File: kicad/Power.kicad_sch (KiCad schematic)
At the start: 40 parts, among them J201 USB_C_2.0, J202 Conn_01x03, U201 RP509Z331B, U202 RP509Z251B, U203 TPS25750DRJK

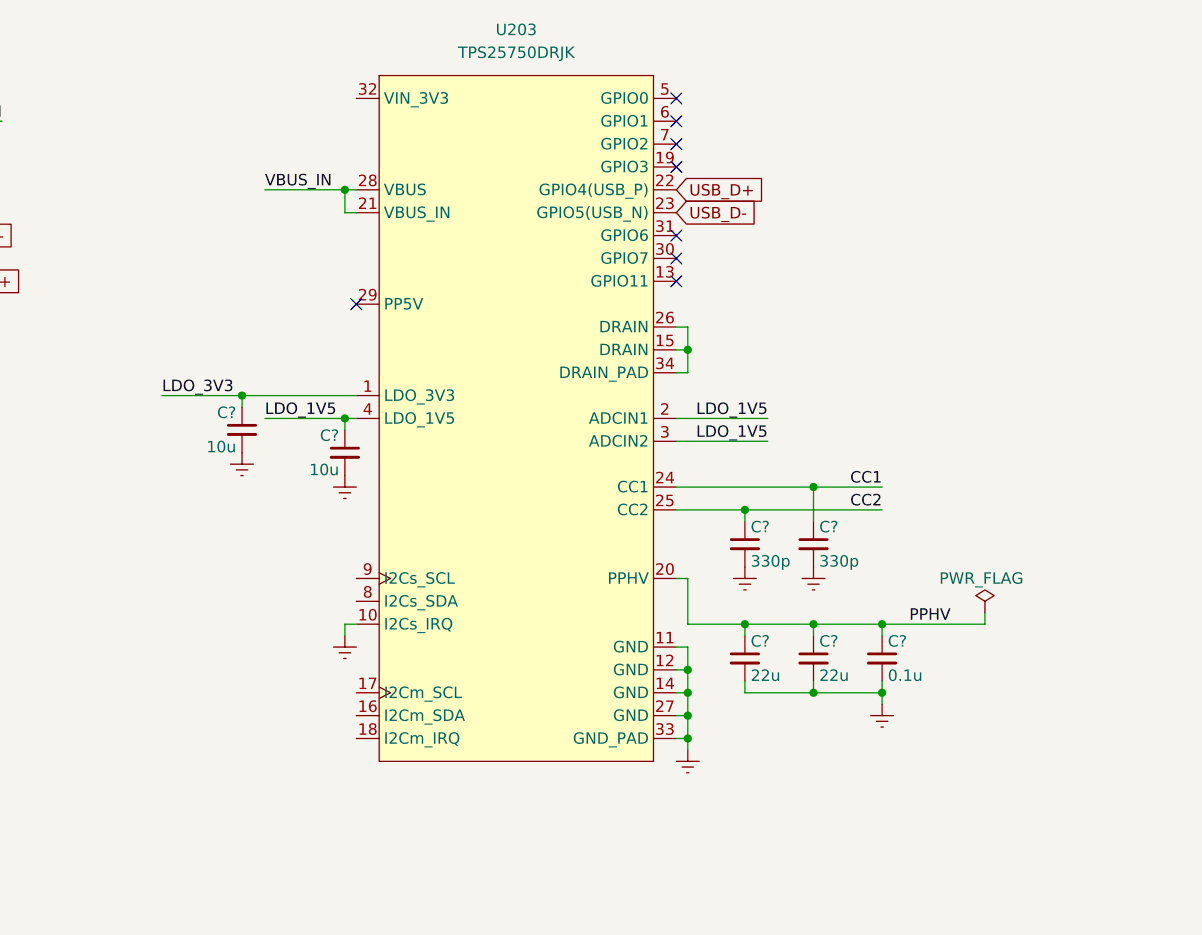
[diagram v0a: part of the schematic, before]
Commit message: rename kicad project files
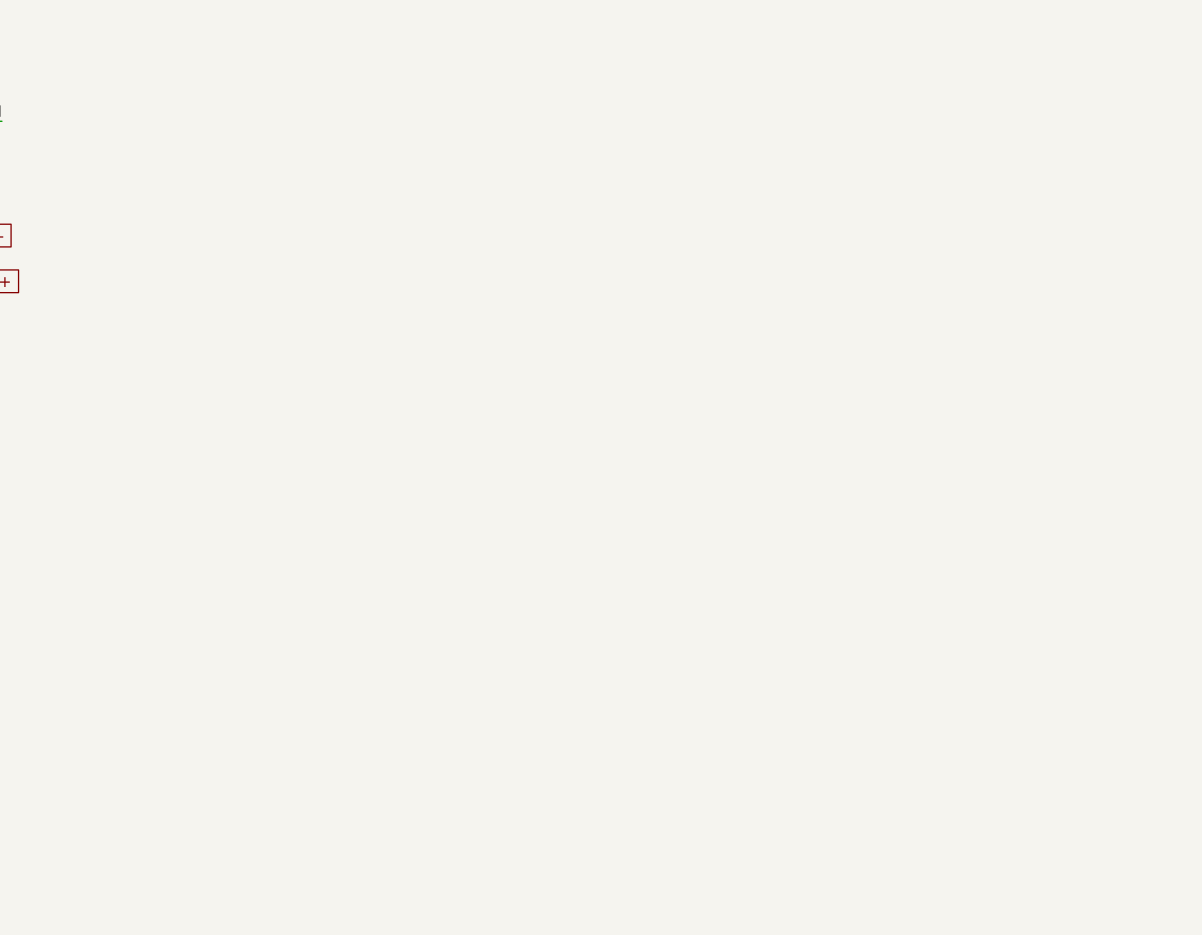
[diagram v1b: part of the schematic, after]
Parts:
- removed C?: 0.1u, Capacitor_SMD:C_0402_1005Metric, symbol Device:C_Small
- removed C? (x2): 22u, Capacitor_SMD:C_0402_1005Metric, symbol Device:C_Small
- removed C? (x2): 10u, Capacitor_SMD:C_0402_1005Metric, symbol Device:C_Small
- removed C? (x2): 330p, Capacitor_SMD:C_0402_1005Metric, symbol Device:C_Small
- removed U203: TPS25750DRJK, clock:POWERWQFN-40, symbol Clock:TPS25750DRJK
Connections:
- no-connect marks 15 -> 7
